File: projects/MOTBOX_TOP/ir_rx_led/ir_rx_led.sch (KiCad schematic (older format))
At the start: 2 parts, among them J1 Conn_01x02

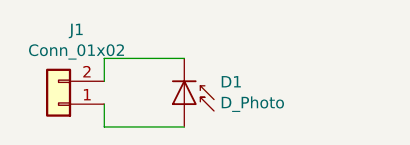
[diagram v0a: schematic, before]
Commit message: New library files and schematics with ESE31 and DT045 switches
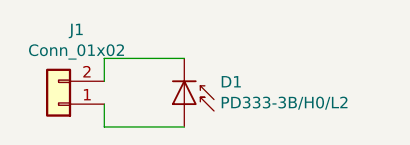
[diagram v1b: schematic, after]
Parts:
- D1: value D_Photo -> PD333-3B/H0/L2
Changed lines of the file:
@@
 P 5000 2500
 F 0 "D1" V 4904 2657 50  0000 L CNN
-F 1 "D_Photo" V 4995 2657 50  0000 L CNN
+F 1 "PD333-3B/H0/L2" V 4995 2657 50  0000 L CNN
 F 2 "LED_THT:LED_D5.0mm_Horizontal_O6.35mm_Z9.0mm" H 4950 2500 50  0001 C CNN
 F 3 "~" H 4950 2500 50  0001 C CNN
